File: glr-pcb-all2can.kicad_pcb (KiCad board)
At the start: 4 copper layers, 64 x 40 mm, 31 parts, among them IC1 TLE6250GV33XUMA1, IC2 ZMR330FTA, IC3 AP64060WU-7, J1 DA15_Pins_MountingHoles, J2 Conn_02x04_Top_Bottom, J3 Conn_01x04, Q1 DMN6075S, Q2 DMN6075S, Q3 DMN6075S, Q4 DMN6075S, U1 STM32F303K8T6

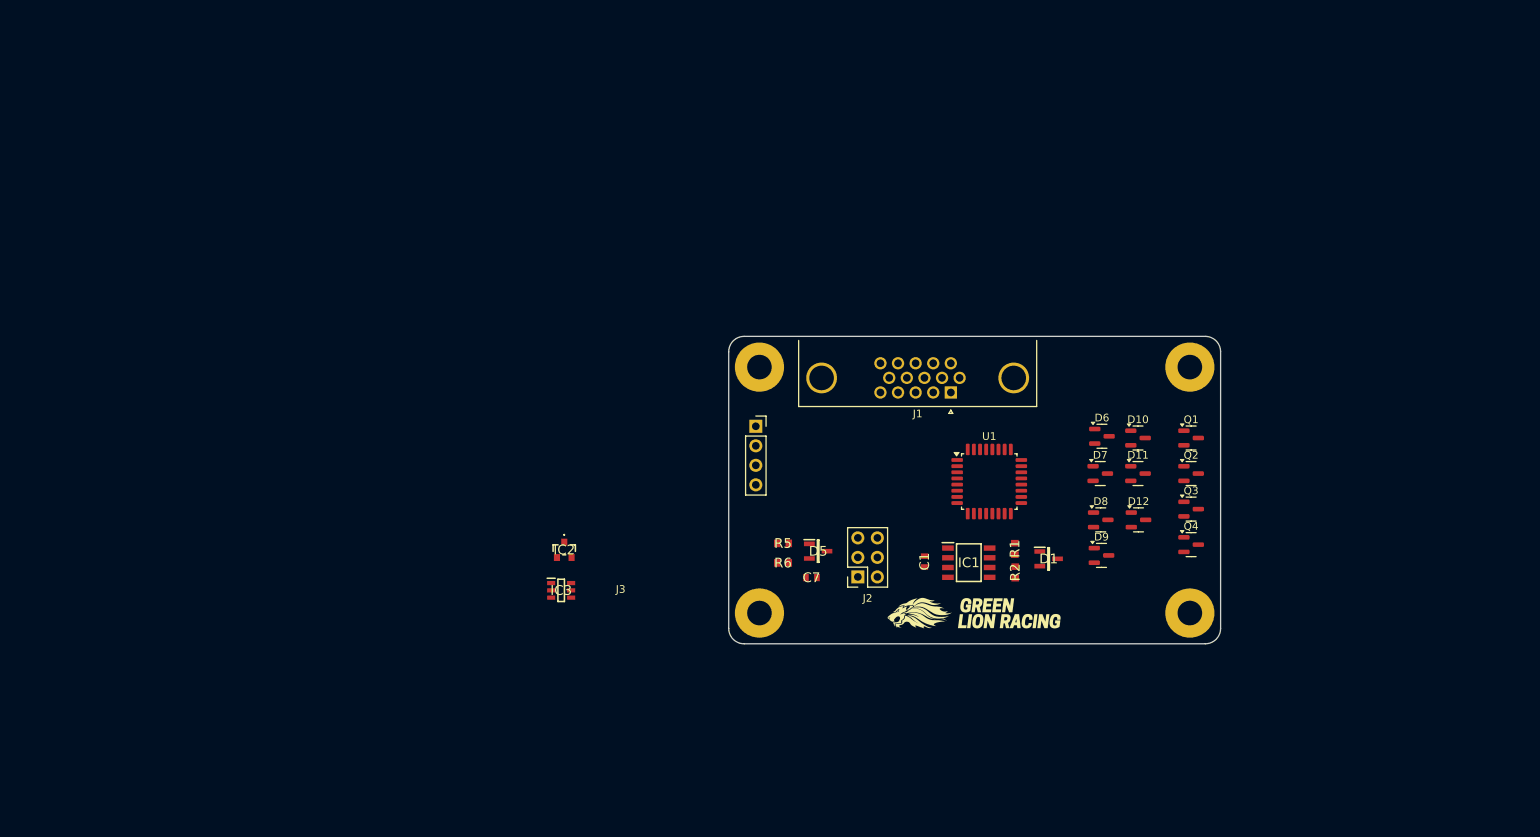
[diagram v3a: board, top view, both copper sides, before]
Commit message: group parts on pcb
replace footprints
update can setup
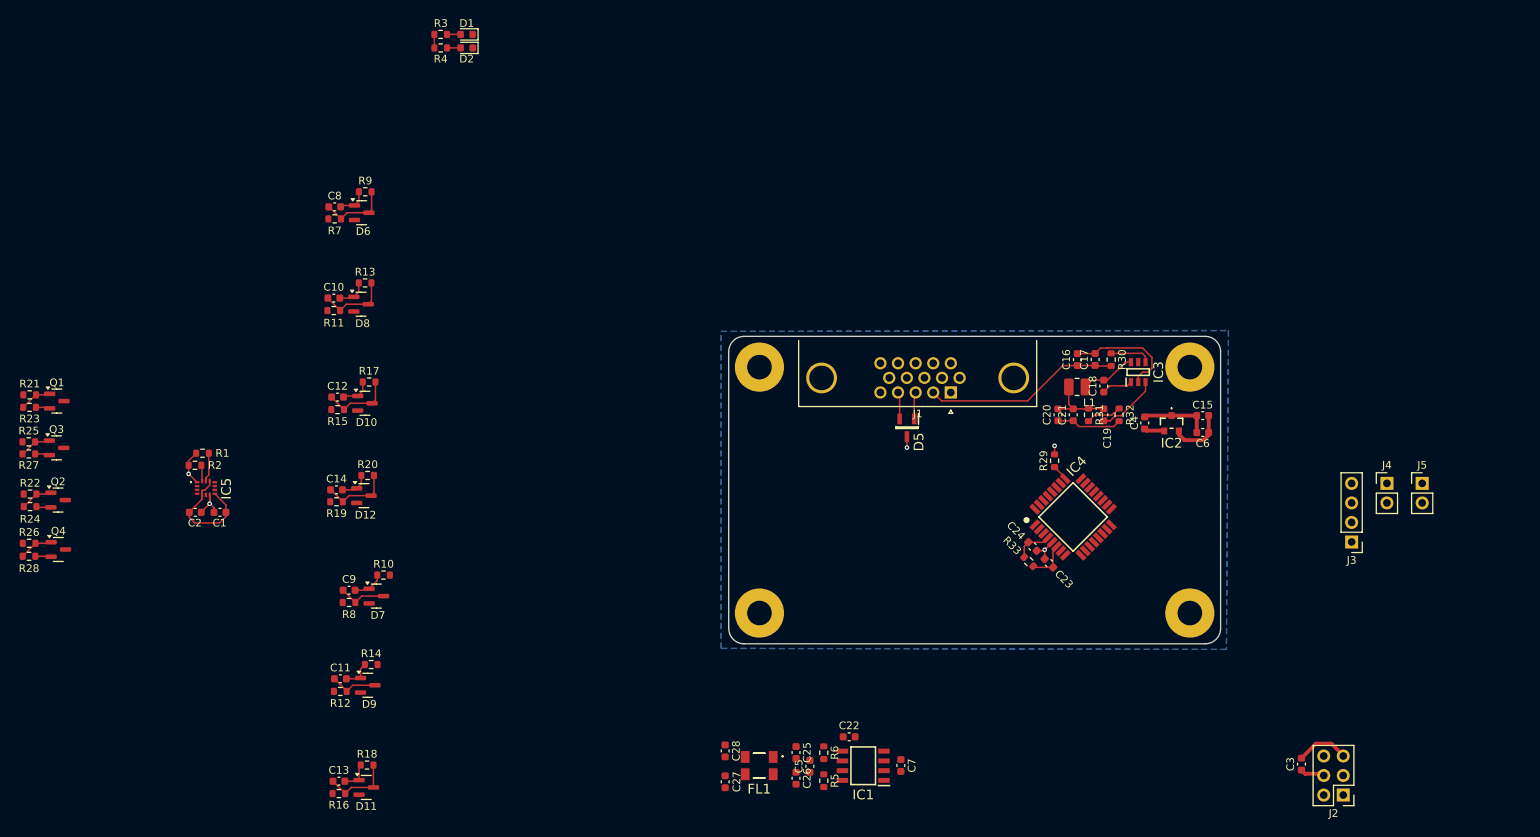
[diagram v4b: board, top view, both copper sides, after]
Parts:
- removed U1: STM32F303K8T6, Package_QFP:LQFP-32_7x7mm_P0.8mm
- added C10: 100n, Capacitor_SMD:C_0603_1608Metric, F.Cu at (66.6, 85.0)
- added C11: 100n, Capacitor_SMD:C_0603_1608Metric, F.Cu at (67.5, 134.6)
- added C12: 100n, Capacitor_SMD:C_0603_1608Metric, F.Cu at (67.1, 97.9)
- added C13: 100n, Capacitor_SMD:C_0603_1608Metric, F.Cu at (67.3, 147.9)
- added C14: 100n, Capacitor_SMD:C_0603_1608Metric, F.Cu at (67.0, 110.0)
- added C15: 100n, Capacitor_SMD:C_0603_1608Metric, F.Cu at (179.7, 100.3)
- added C16: 2u2, Capacitor_SMD:C_0603_1608Metric, F.Cu at (163.4, 93.0)
- added C17: 100n, Capacitor_SMD:C_0603_1608Metric, F.Cu at (165.7, 93.0)
- added C18: 100n, Capacitor_SMD:C_0603_1608Metric, F.Cu at (166.8, 96.5)
- added C19: 100n, Capacitor_SMD:C_0603_1608Metric, F.Cu at (166.8, 100.2)
- added C2: 100n, Capacitor_SMD:C_0603_1608Metric, F.Cu at (48.6, 112.9)
- added C20: 1u, Capacitor_SMD:C_0603_1608Metric, F.Cu at (160.8, 100.2)
- added C21: 100n, Capacitor_SMD:C_0603_1608Metric, F.Cu at (162.8, 100.2)
- added C22: 100n, Capacitor_SMD:C_0603_1608Metric, F.Cu at (133.7, 142.1)
- added C23: 100n, Capacitor_SMD:C_0603_1608Metric, F.Cu at (159.7, 119.5)
- added C24: 1u, Capacitor_SMD:C_0603_1608Metric, F.Cu at (157.5, 117.3)
- added C25: 100p, Capacitor_SMD:C_0603_1608Metric, F.Cu at (126.8, 144.1)
- added C26: 100p, Capacitor_SMD:C_0603_1608Metric, F.Cu at (126.8, 147.5)
- added C27: 100p, Capacitor_SMD:C_0603_1608Metric, F.Cu at (117.5, 148.0)
- added C28: 100p, Capacitor_SMD:C_0603_1608Metric, F.Cu at (117.5, 143.9)
- added C3: 100n, Capacitor_SMD:C_0603_1608Metric, F.Cu at (192.5, 145.7)
- added C4: 10u, Capacitor_SMD:C_0603_1608Metric, F.Cu at (172.1, 101.3)
- added C5: 100n, Capacitor_SMD:C_0603_1608Metric, F.Cu at (128.6, 145.9)
- added C6: 10u, Capacitor_SMD:C_0603_1608Metric, F.Cu at (179.7, 102.5)
- added C8: 100n, Capacitor_SMD:C_0603_1608Metric, F.Cu at (66.7, 73.2)
- added C9: 100n, Capacitor_SMD:C_0603_1608Metric, F.Cu at (68.6, 123.0)
- added D2: LED, LED_SMD:LED_0603_1608Metric, F.Cu at (83.9, 52.5)
- added FL1: Choke, SamacSys_Parts:744235510, F.Cu at (122.0, 145.8)
- added IC4: STM32C092KCT6, SamacSys_Parts:QFP80P900X900X160-32N, F.Cu at (162.8, 113.5)
- added IC5: LSM6DSV16BXTR, SamacSys_Parts:LSM6DSV16BXTR, F.Cu at (50.0, 109.7)
- added J4: Conn_01x02, Connector_PinHeader_2.54mm:PinHeader_1x02_P2.54mm_Vertical, F.Cu at (203.6, 109.1)
- added J5: Conn_01x02, Connector_PinHeader_2.54mm:PinHeader_1x02_P2.54mm_Vertical, F.Cu at (208.2, 109.1)
- added L1: 10u, Inductor_SMD:L_1008_2520Metric, F.Cu at (163.3, 96.6)
- added R10: ~, Resistor_SMD:R_0603_1608Metric, F.Cu at (73.1, 121.1)
- added R11: 30k, Resistor_SMD:R_0603_1608Metric, F.Cu at (66.6, 86.6)
- added R12: 30k, Resistor_SMD:R_0603_1608Metric, F.Cu at (67.5, 136.2)
- added R13: ~, Resistor_SMD:R_0603_1608Metric, F.Cu at (70.7, 83.0)
- added R14: ~, Resistor_SMD:R_0603_1608Metric, F.Cu at (71.5, 132.7)
- added R15: 30k, Resistor_SMD:R_0603_1608Metric, F.Cu at (67.1, 99.5)
- added R16: 30k, Resistor_SMD:R_0603_1608Metric, F.Cu at (67.3, 149.5)
- added R17: ~, Resistor_SMD:R_0603_1608Metric, F.Cu at (71.2, 95.9)
- added R18: ~, Resistor_SMD:R_0603_1608Metric, F.Cu at (70.9, 145.8)
- added R19: 30k, Resistor_SMD:R_0603_1608Metric, F.Cu at (67.0, 111.5)
- added R20: ~, Resistor_SMD:R_0603_1608Metric, F.Cu at (71.0, 108.1)
- added R21: 200, Resistor_SMD:R_0603_1608Metric, F.Cu at (27.0, 97.6)
- added R22: 200, Resistor_SMD:R_0603_1608Metric, F.Cu at (27.1, 110.5)
- added R23: 10k, Resistor_SMD:R_0603_1608Metric, F.Cu at (27.0, 99.2)
- added R24: 10k, Resistor_SMD:R_0603_1608Metric, F.Cu at (27.1, 112.1)
- added R25: 200, Resistor_SMD:R_0603_1608Metric, F.Cu at (26.9, 103.7)
- added R26: 200, Resistor_SMD:R_0603_1608Metric, F.Cu at (27.0, 116.9)
- added R27: 10k, Resistor_SMD:R_0603_1608Metric, F.Cu at (26.9, 105.3)
- added R28: 10k, Resistor_SMD:R_0603_1608Metric, F.Cu at (27.0, 118.6)
- added R29: 120, Resistor_SMD:R_0603_1608Metric, F.Cu at (160.4, 106.2)
- added R3: 120, Resistor_SMD:R_0603_1608Metric, F.Cu at (80.5, 50.7)
- added R30: 10k, Resistor_SMD:R_0603_1608Metric, F.Cu at (167.8, 93.0)
- added R31: 51, Resistor_SMD:R_0603_1608Metric, F.Cu at (164.8, 100.2)
- added R32: 10, Resistor_SMD:R_0603_1608Metric, F.Cu at (168.8, 100.2)
- added R33: 100k, Resistor_SMD:R_0603_1608Metric, F.Cu at (157.0, 119.3)
- added R4: 120, Resistor_SMD:R_0603_1608Metric, F.Cu at (80.5, 52.5)
- added R7: 30k, Resistor_SMD:R_0603_1608Metric, F.Cu at (66.7, 74.7)
- added R8: 30k, Resistor_SMD:R_0603_1608Metric, F.Cu at (68.6, 124.6)
- added R9: ~, Resistor_SMD:R_0603_1608Metric, F.Cu at (70.7, 71.2)
- C1: value 1uF -> 100n; footprint SamacSys_Parts:CAPC1608X90N -> Capacitor_SMD:C_0603_1608Metric
- C7: value 0.1μF 50V -> 100n; footprint SamacSys_Parts:CAPC1608X90N -> Capacitor_SMD:C_0603_1608Metric
- D1: footprint SamacSys_Parts:SOT95P255X125-3N -> LED_SMD:LED_0603_1608Metric
- G***: moved to B.Cu
- IC1: value TLE6250GV33XUMA1 -> ATA6561-GAQW-N
- J2: value Conn_02x04_Top_Bottom -> Conn_02x03_Top_Bottom; footprint Connector_PinSocket_2.54mm:PinSocket_2x03_P2.54mm_Vertical -> Connector_PinHeader_2.54mm:PinHeader_2x03_P2.54mm_Vertical
- J3: footprint Connector_PinSocket_2.54mm:PinSocket_1x04_P2.54mm_Vertical -> Connector_PinHeader_2.54mm:PinHeader_1x04_P2.54mm_Vertical
- R1: footprint SamacSys_Parts:RESC1608X50N -> Resistor_SMD:R_0603_1608Metric
- R2: value 120R -> 100k; footprint SamacSys_Parts:RESC1608X50N -> Resistor_SMD:R_0603_1608Metric
- R5, R6: value 120.0 Ω -> 60; footprint SamacSys_Parts:RESC1608X50N -> Resistor_SMD:R_0603_1608Metric
- moved Q3 147.8 mm to (30.5, 104.5)
- moved Q1 147.7 mm to (30.6, 98.4)
- moved Q2 147.5 mm to (30.7, 111.3)
- moved Q4 147.4 mm to (30.8, 117.7)
- moved D11 108.4 mm to (70.8, 148.7)
- moved R2 107.6 mm to (48.6, 106.8), turned to 0 degrees
- moved R1 106.4 mm to (49.5, 105.2), turned to 0 degrees
- moved D1 101.9 mm to (83.9, 50.7), turned to 180 degrees
- moved D12 100.8 mm to (70.5, 110.7)
- moved D10 100.7 mm to (70.7, 98.7)
- moved D6 100.6 mm to (70.2, 73.9)
- moved D8 100.2 mm to (70.2, 85.8)
- moved D9 96.9 mm to (71.0, 135.4)
- moved D7 95.5 mm to (72.2, 123.8)
- moved C1 91.9 mm to (51.8, 112.9), turned to 0 degrees
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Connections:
- D1 pad 1: Net-(D1-K) -> LED_1
- D10 pad 3: /Input filter/3_IN -> IC_IN_3
- D11 pad 3: /Input filter/7_IN_INT -> IC_IN_7
- D12 pad 3: /Input filter/4_IN_INT -> IC_IN_4
- D5 pad 1: /CAN transciever/CAN H 1 -> /CAN transciever/CAN L 1
- D5 pad 2: /CAN transciever/CAN L 1 -> /CAN transciever/CAN H 1
- D6 pad 3: /Input filter/1_IN_INT -> IC_IN_1
- D7 pad 3: /Input filter/5_IN_INT -> IC_IN_5
- D8 pad 3: /Input filter/2_IN_INT -> IC_IN_2
- D9 pad 3: /Input filter/6_IN_INT -> IC_IN_6
- IC1 pad 1: /CAN transciever/TX 1 -> FDCAN1_TX
- IC1 pad 4: /CAN transciever/RX 1 -> FDCAN1_RX
- IC2 pad 1: unconnected-(IC2-GND-Pad1) -> GND
- IC2 pad 2: unconnected-(IC2-OUT-Pad2) -> +3V3
- IC2 pad 3: unconnected-(IC2-IN-Pad3) -> +5V
- IC3 pad 1: unconnected-(IC3-BST-Pad1) -> Net-(IC3-BST)
- IC3 pad 2: unconnected-(IC3-GND-Pad2) -> GND
- IC3 pad 3: unconnected-(IC3-FB-Pad3) -> Net-(IC3-FB)
- IC3 pad 4: unconnected-(IC3-EN-Pad4) -> Net-(IC3-EN)
- IC3 pad 5: unconnected-(IC3-VIN-Pad5) -> +24V
- IC3 pad 6: unconnected-(IC3-SW-Pad6) -> Net-(IC3-SW)
- J1 pad 12: 1_OUT -> /Output/4_OUT
- J1 pad 13: 2_OUT -> /Output/3_OUT
- J1 pad 14: 3_OUT -> /Output/2_OUT
- J1 pad 15: 4_OUT -> /Output/1_OUT
- J2 pad 1: Net-(J2-Pin_1) -> SWCLK
- J2 pad 2: Net-(J2-Pin_2) -> SWDIO
- J3 pad 1: Net-(J3-Pin_1) -> SPI1_NSS
- J3 pad 2: Net-(J3-Pin_2) -> SPI1_SCK
- J3 pad 3: Net-(J3-Pin_3) -> SPI1_MISO
- J3 pad 4: Net-(J3-Pin_4) -> SPI1_MOSI
- Q1 pad 3: 1_OUT -> /Output/1_OUT
- Q2 pad 3: 3_OUT -> /Output/3_OUT
- Q3 pad 3: 2_OUT -> /Output/2_OUT
- Q4 pad 3: 4_OUT -> /Output/4_OUT
- R1 pad 1: +3V3 -> GND
- R1 pad 2: NRST -> I2C1_SCL
- R2 pad 1: Net-(U1-BOOT0) -> GND
- R2 pad 2: GND -> I2C1_SDA
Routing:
- net GND: track 0.00 -> 88.6 mm, vias 0 -> 5
- net +3V3: track 0.00 -> 31.2 mm
- net +24V: track 0.00 -> 25.5 mm
- net +5V: track 0.00 -> 16.5 mm
- net IC_IN_7: track 0.00 -> 9.35 mm
- net IC_IN_3: track 0.00 -> 9.25 mm
- net IC_IN_2: track 0.00 -> 9.22 mm
- net IC_IN_1: track 0.00 -> 9.07 mm
- net IC_IN_4: track 0.00 -> 9.03 mm
- net Net-(IC3-FB): track 0.00 -> 8.21 mm
- net Net-(IC3-SW): track 0.00 -> 7.26 mm
- net IC_IN_6: track 0.00 -> 6.33 mm
- net IC_IN_5: track 0.00 -> 6.26 mm
- net NRST: track 0.00 -> 5.56 mm
- net Net-(IC3-EN): track 0.00 -> 5.37 mm
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- added copper zone on B.Cu, net GND

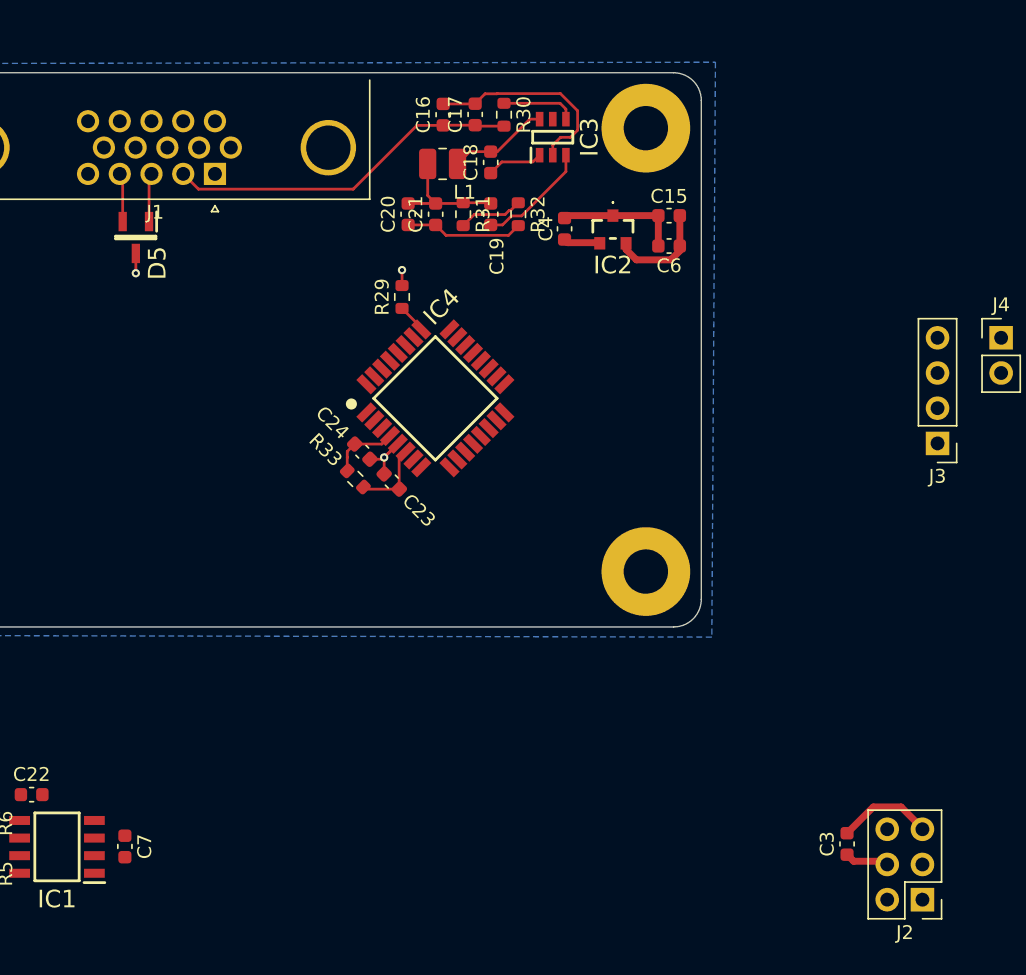
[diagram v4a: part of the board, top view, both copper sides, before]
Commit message: change swd header
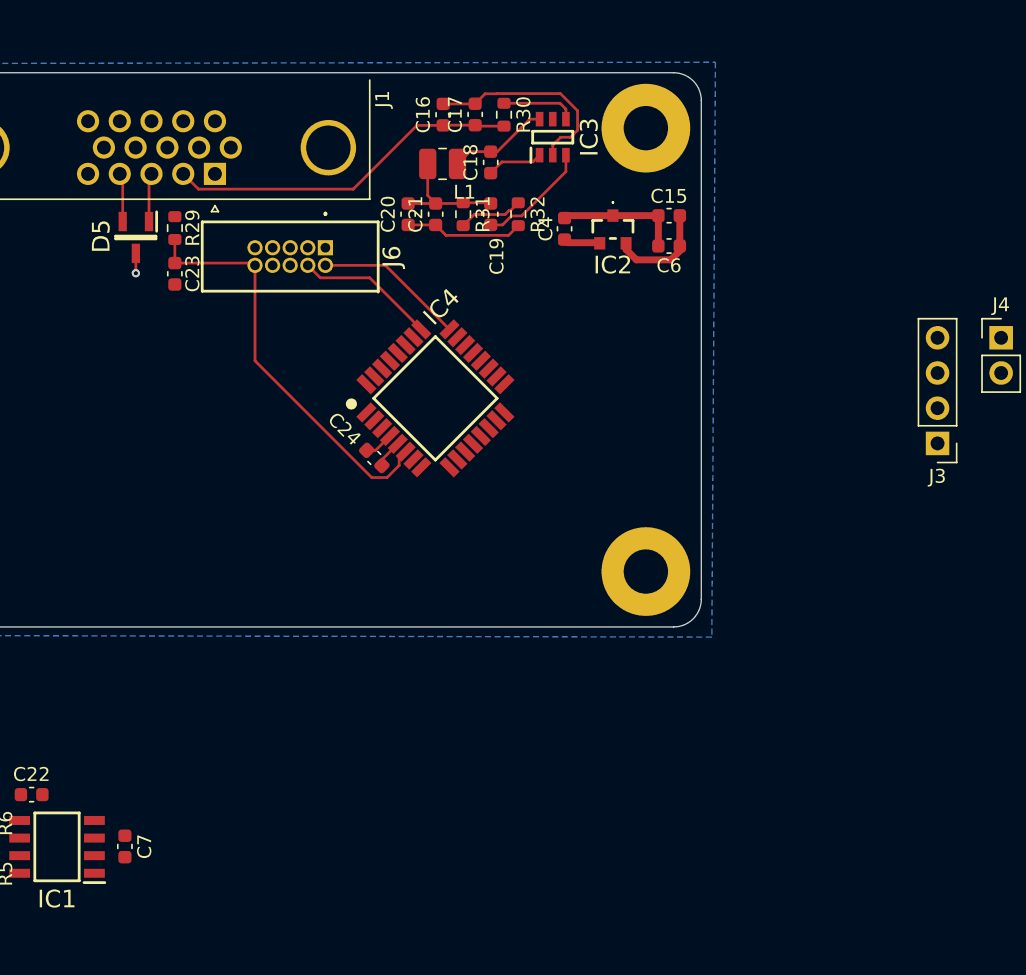
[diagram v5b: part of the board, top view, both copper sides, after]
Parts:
- removed C3: 100n, Capacitor_SMD:C_0603_1608Metric
- removed J2: Conn_02x03_Top_Bottom, Connector_PinHeader_2.54mm:PinHeader_2x03_P2.54mm_Vertical
- removed R33: 100k, Resistor_SMD:R_0603_1608Metric
- added J6: 62701021621, SamacSys_Parts:62701021621, F.Cu at (154.9, 102.6)
- R1, R2: value 100k -> 10k
- R29: value 120 -> 10k
- moved C23 21.7 mm to (144.0, 104.5), turned to 90 degrees
- moved R29 17.1 mm to (144.0, 101.2)
- moved G*** 7.42 mm to (142.6, 125.5)
- moved C24 0.98 mm to (158.4, 117.8)
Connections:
- R1 pad 1: GND -> +3V3
- R2 pad 1: GND -> +3V3
- R29 pad 1: SWCLK -> NRST
- R29 pad 2: GND -> +3V3
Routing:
- net NRST: track 5.56 -> 29.9 mm
- net SWDIO: track 0.00 -> 10.9 mm
- net +3V3: track 31.2 -> 21.5 mm
- net SWCLK: track 2.09 -> 10.2 mm
- net GND: track 88.6 -> 81.3 mm, vias 5 -> 3
